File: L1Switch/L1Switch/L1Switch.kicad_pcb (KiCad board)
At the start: 4 copper layers, 191 parts, among them J1 RJSNEGF8A08, J2 Conn_01x07_Male, J3 Barrel_Jack, T1 SM51589PEL, T2 SM51589PEL, T3 SM51589PEL, T4 SM51589PEL, T5 SM51589PEL, T6 SM51589PEL, T7 SM51589PEL, T8 SM51589PEL, U1 XC7A15T-FTG256, U2 VSC8658, U3 TPS548A20RVE, U4 TPS565208, U5 TPS565208, U6 TPS565208

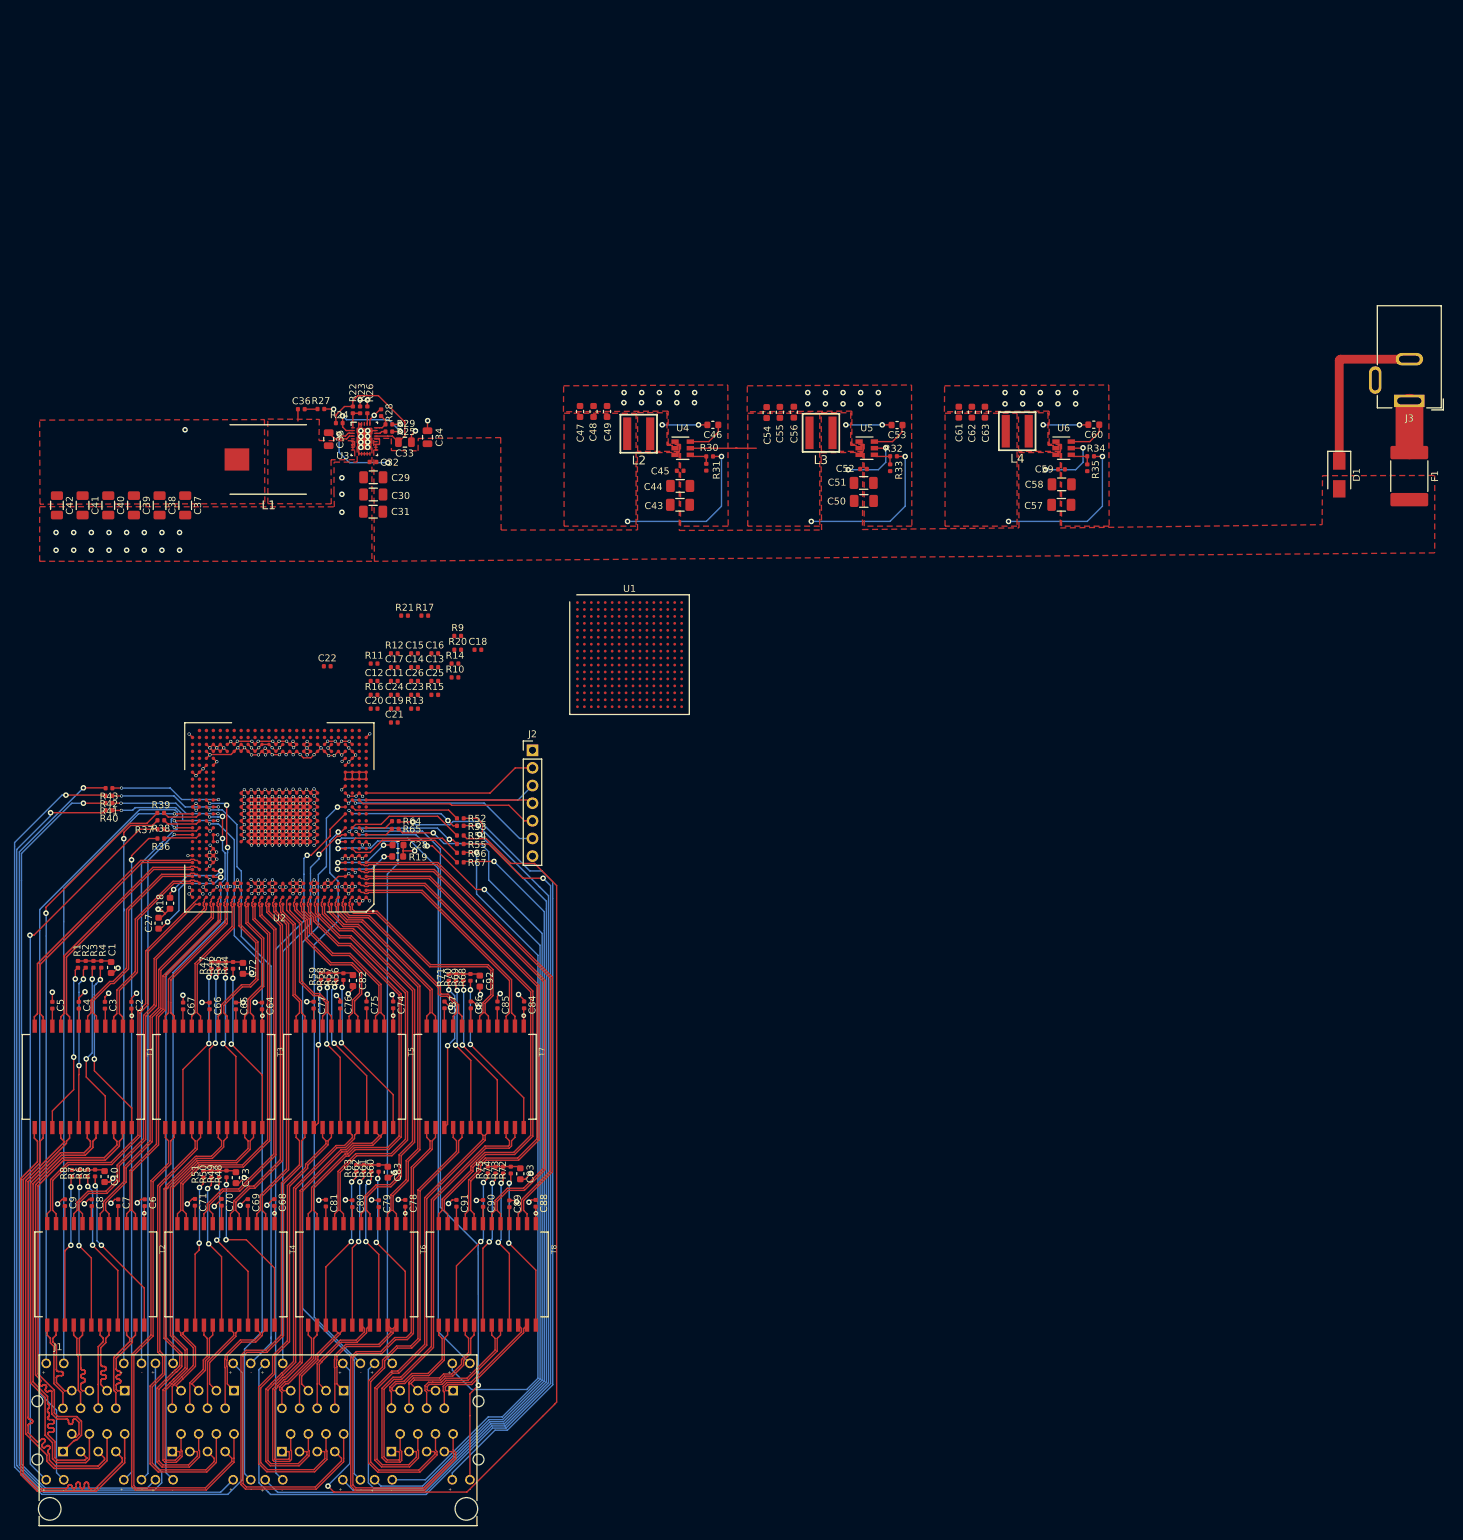
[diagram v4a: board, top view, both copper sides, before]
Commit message: SGMII 0 Rx/Tx routed to FPGA.
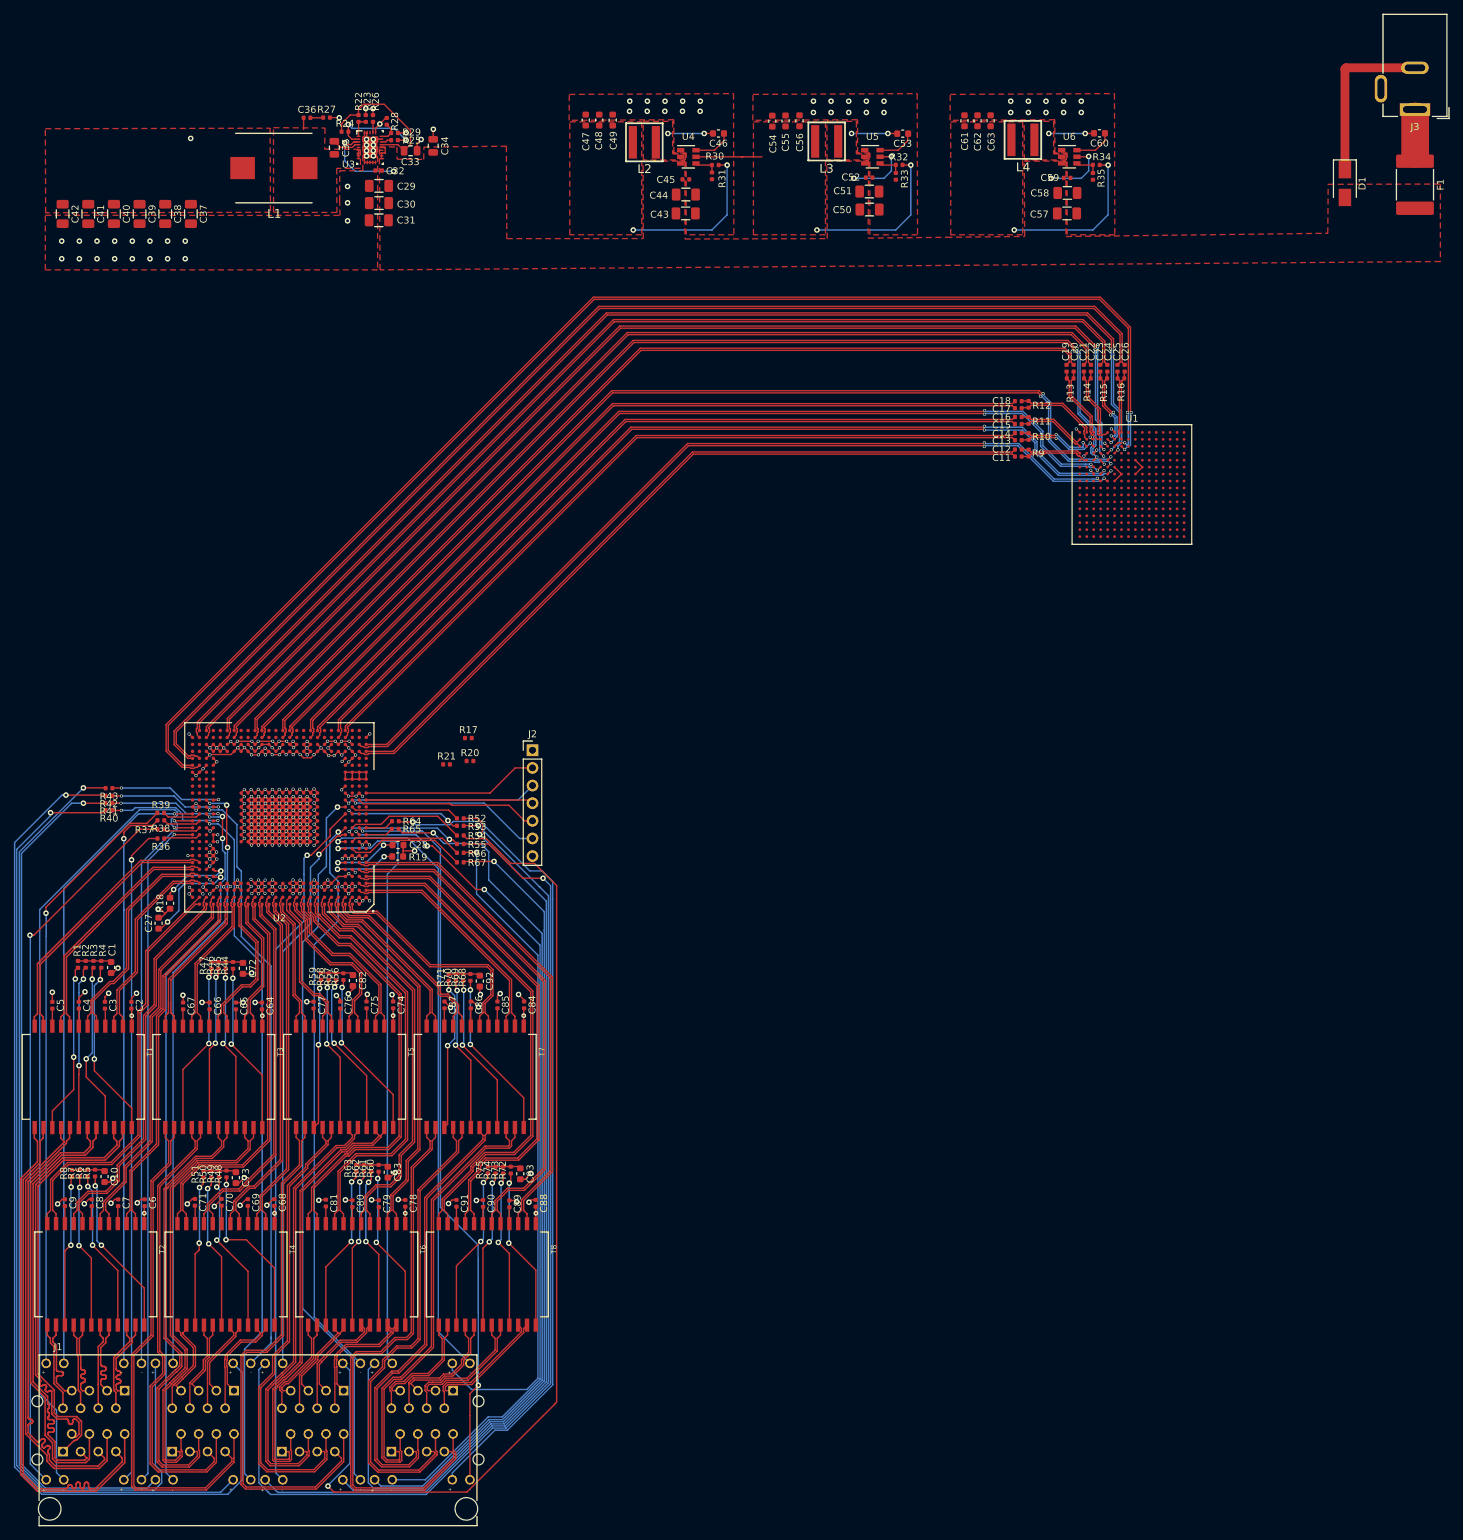
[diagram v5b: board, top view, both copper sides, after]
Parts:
- moved C22 118.0 mm to (224.1, -11.7), turned to 90 degrees
- moved R16 116.7 mm to (228.4, -10.3), turned to 180 degrees
- moved C24 112.9 mm to (226.5, -11.7), turned to 90 degrees
- moved C20 112.0 mm to (221.6, -11.7), turned to 90 degrees
- moved C26 111.7 mm to (229.0, -11.7), turned to 90 degrees
- moved C21 111.6 mm to (223.1, -11.7), turned to 90 degrees
- moved C23 109.3 mm to (225.4, -11.7), turned to 90 degrees
- moved C19 108.5 mm to (220.6, -11.7), turned to 90 degrees
- moved C25 108.1 mm to (227.9, -11.7), turned to 90 degrees
- moved R15 106.5 mm to (225.9, -10.3), turned to 180 degrees
- moved R13 105.7 mm to (221.1, -10.3), turned to 180 degrees
- moved R11 100.5 mm to (215.1, -4.22), turned to -90 degrees
- moved R14 99.9 mm to (223.6, -10.3), turned to 180 degrees
- moved C12 98.5 mm to (213.6, -0.04), turned to 180 degrees
- moved R12 98.1 mm to (215.1, -6.54), turned to -90 degrees
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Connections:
- net Net-(C11-Pad2) renamed /Net 1/RD_P7
- net Net-(C12-Pad2) renamed /Net 1/RD_N7
- net Net-(C13-Pad2) renamed /Net 1/RD_P6
- net Net-(C14-Pad2) renamed /Net 1/RD_N6
- net Net-(C15-Pad2) renamed /Net 1/RD_P5
- net Net-(C16-Pad2) renamed /Net 1/RD_N5
- net Net-(C17-Pad2) renamed /Net 1/RD_P4
- net Net-(C18-Pad2) renamed /Net 1/RD_N4
- net Net-(C19-Pad2) renamed /Net 1/RD_P3
- net Net-(C20-Pad2) renamed /Net 1/RD_N3
- net Net-(C21-Pad2) renamed /Net 1/RD_P2
- net Net-(C22-Pad2) renamed /Net 1/RD_N2
- net Net-(C23-Pad2) renamed /Net 1/RD_P1
- net Net-(C24-Pad2) renamed /Net 1/RD_N1
- net Net-(C25-Pad2) renamed /Net 1/RD_P0
- net Net-(C26-Pad2) renamed /Net 1/RD_N0
- C24 pad 1: /SGMII.RD_P0 -> /SGMII.RD_N1
- C25 pad 1: /SGMII.RD_N1 -> /SGMII.RD_P0
- R15 pad 1: /SGMII.RD_P0 -> /SGMII.RD_N1
- R16 pad 2: /SGMII.RD_N1 -> /SGMII.RD_P0
- U1 pad A2: Net-(U1-PadA2) -> /SGMII.RD_N4
- U1 pad A3: Net-(U1-PadA3) -> /SGMII.RD_N3
- U1 pad A4: Net-(U1-PadA4) -> /SGMII.RD_N2
- U1 pad A5: Net-(U1-PadA5) -> /SGMII.RD_P2
- U1 pad A7: Net-(U1-PadA7) -> /SGMII.RD_N0
- U1 pad B1: Net-(U1-PadB1) -> /SGMII.RD_N5
- U1 pad B2: Net-(U1-PadB2) -> /SGMII.RD_P4
- U1 pad B4: Net-(U1-PadB4) -> /SGMII.RD_P3
- U1 pad B5: Net-(U1-PadB5) -> /SGMII.RD_N1
- U1 pad B6: Net-(U1-PadB6) -> /SGMII.RD_P1
- U1 pad B7: Net-(U1-PadB7) -> /SGMII.RD_P0
- U1 pad C1: Net-(U1-PadC1) -> /SGMII.RD_P5
- U1 pad C2: Net-(U1-PadC2) -> /SGMII.RD_N6
- U1 pad C3: Net-(U1-PadC3) -> /SGMII.RD_P6
- U1 pad C4: Net-(U1-PadC4) -> /SGMII.TD_N2
- U1 pad C6: Net-(U1-PadC6) -> /SGMII.TD_N0
- U1 pad C7: Net-(U1-PadC7) -> /SGMII.TD_P0
- U1 pad D1: Net-(U1-PadD1) -> /SGMII.RD_N7
- U1 pad D16: /SGMII.RD_N7 -> Net-(U1-PadD16)
- U1 pad D3: Net-(U1-PadD3) -> /SGMII.TD_N3
- U1 pad D4: Net-(U1-PadD4) -> /SGMII.TD_P2
- U1 pad D5: Net-(U1-PadD5) -> /SGMII.TD_N1
- U1 pad D6: Net-(U1-PadD6) -> /SGMII.TD_P1
- U1 pad E15: /SGMII.RD_N6 -> Net-(U1-PadE15)
- U1 pad E16: /SGMII.RD_P7 -> Net-(U1-PadE16)
- U1 pad E2: Net-(U1-PadE2) -> /SGMII.RD_P7
- U1 pad E3: Net-(U1-PadE3) -> /SGMII.TD_P3
- U1 pad E5: Net-(U1-PadE5) -> /SGMII.TD_N4
- U1 pad F14: /SGMII.RD_N3 -> Net-(U1-PadF14)
- U1 pad F15: /SGMII.RD_P6 -> Net-(U1-PadF15)
- U1 pad F3: Net-(U1-PadF3) -> /SGMII.TD_N5
- U1 pad F4: Net-(U1-PadF4) -> /SGMII.TD_P5
- U1 pad F5: Net-(U1-PadF5) -> /SGMII.TD_P4
- U1 pad G12: /SGMII.RD_N5 -> Net-(U1-PadG12)
- U1 pad G14: /SGMII.RD_P3 -> Net-(U1-PadG14)
- U1 pad G15: /SGMII.RD_N0 -> Net-(U1-PadG15)
- U1 pad G16: /SGMII.RD_N2 -> Net-(U1-PadG16)
- U1 pad G4: Net-(U1-PadG4) -> /SGMII.TD_N6
- U1 pad G5: Net-(U1-PadG5) -> /SGMII.TD_P6
- U1 pad H11: /SGMII.RD_P5 -> Net-(U1-PadH11)
- U1 pad H12: /SGMII.RD_P4 -> Net-(U1-PadH12)
- U1 pad H13: /SGMII.RD_N4 -> Net-(U1-PadH13)
- U1 pad H14: /SGMII.RD_P0 -> Net-(U1-PadH14)
- U1 pad H16: /SGMII.RD_P2 -> Net-(U1-PadH16)
- U1 pad H4: Net-(U1-PadH4) -> /SGMII.TD_N7
- U1 pad H5: Net-(U1-PadH5) -> /SGMII.TD_P7
- U1 pad J15: /SGMII.RD_P1 -> Net-(U1-PadJ15)
- U1 pad J16: /SGMII.RD_N1 -> Net-(U1-PadJ16)
- U1 pad M6: /SGMII.TD_P5 -> Net-(U1-PadM6)
- U1 pad N6: /SGMII.TD_N5 -> Net-(U1-PadN6)
- U1 pad N9: /SGMII.TD_P6 -> Net-(U1-PadN9)
- U1 pad P8: /SGMII.TD_P4 -> Net-(U1-PadP8)
- U1 pad P9: /SGMII.TD_N6 -> Net-(U1-PadP9)
- U1 pad R10: /SGMII.TD_P7 -> Net-(U1-PadR10)
- U1 pad R11: /SGMII.TD_N7 -> Net-(U1-PadR11)
- U1 pad R5: /SGMII.TD_P1 -> Net-(U1-PadR5)
- U1 pad R6: /SGMII.TD_P0 -> Net-(U1-PadR6)
- U1 pad R7: /SGMII.TD_N0 -> Net-(U1-PadR7)
- U1 pad R8: /SGMII.TD_N4 -> Net-(U1-PadR8)
- U1 pad T10: /SGMII.TD_N2 -> Net-(U1-PadT10)
- U1 pad T5: /SGMII.TD_N1 -> Net-(U1-PadT5)
- U1 pad T7: /SGMII.TD_P3 -> Net-(U1-PadT7)
- U1 pad T8: /SGMII.TD_N3 -> Net-(U1-PadT8)
- U1 pad T9: /SGMII.TD_P2 -> Net-(U1-PadT9)
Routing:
- net /SGMII.TD_P0: track 0.00 -> 194.7 mm, vias 0 -> 2
- net /SGMII.TD_N0: track 0.00 -> 192.5 mm, vias 0 -> 2
- net /SGMII.TD_P1: track 0.00 -> 177.8 mm, vias 0 -> 2
- net /SGMII.TD_N1: track 0.00 -> 175.8 mm, vias 0 -> 2
- net /Net 1/RD_N0: track 0.00 -> 173.5 mm
- net /Net 1/RD_P0: track 0.00 -> 173.2 mm
- net /SGMII.TD_P2: track 0.00 -> 168.6 mm, vias 0 -> 2
- net /SGMII.TD_N2: track 0.00 -> 167.5 mm, vias 0 -> 2
- net /SGMII.TD_P3: track 0.00 -> 161.4 mm, vias 0 -> 2
- net /SGMII.TD_N3: track 0.00 -> 160.6 mm, vias 0 -> 2
- net /Net 1/RD_P1: track 0.00 -> 159.2 mm
- net /Net 1/RD_N1: track 0.00 -> 159.0 mm
- net /Net 1/RD_P2: track 0.00 -> 150.7 mm
- net /Net 1/RD_N2: track 0.00 -> 150.5 mm
- net /SGMII.TD_P4: track 0.00 -> 149.4 mm, vias 0 -> 2
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
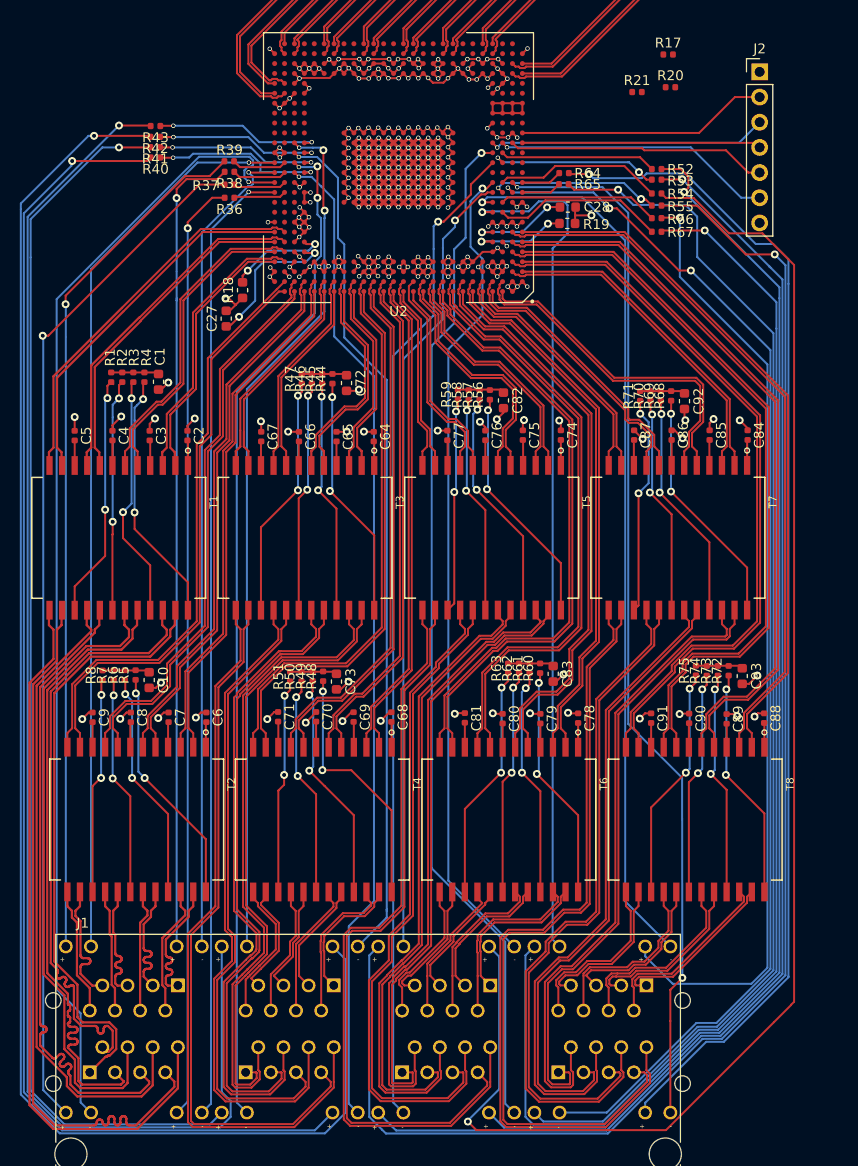
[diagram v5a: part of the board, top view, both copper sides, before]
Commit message: Add decoupling caps and ferrite bead. Clean up reference designators.
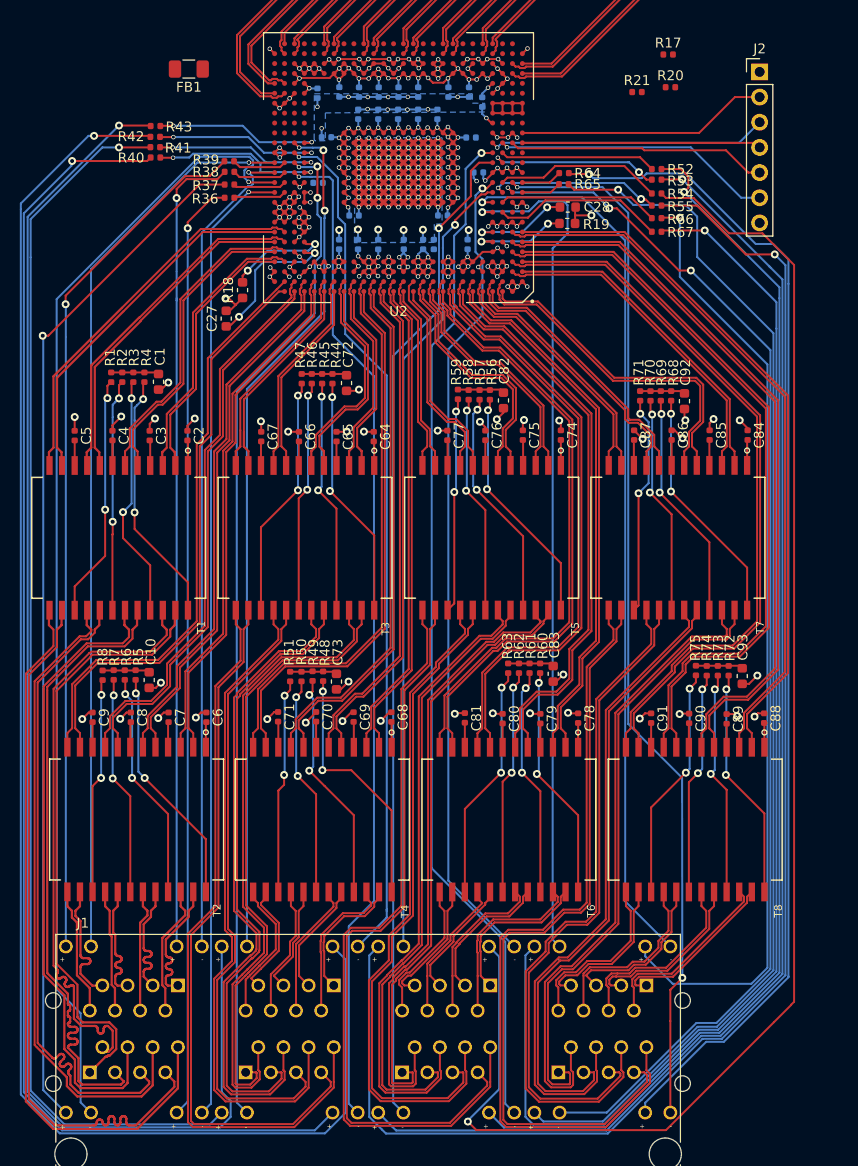
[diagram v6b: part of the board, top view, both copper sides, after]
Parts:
- added C100: 100nF, Capacitor_SMD:C_0402_1005Metric, B.Cu at (107.3, 45.3)
- added C101: 100nF, Capacitor_SMD:C_0402_1005Metric, B.Cu at (101.3, 60.7)
- added C102: 100nF, Capacitor_SMD:C_0402_1005Metric, B.Cu at (114.6, 49.9)
- added C103: 100nF, Capacitor_SMD:C_0402_1005Metric, B.Cu at (105.2, 47.5)
- added C104: 100nF, Capacitor_SMD:C_0402_1005Metric, B.Cu at (109.2, 47.5)
- added C105: 100nF, Capacitor_SMD:C_0402_1005Metric, B.Cu at (111.2, 47.5)
- added C106: 100nF, Capacitor_SMD:C_0402_1005Metric, B.Cu at (107.2, 47.5)
- added C107: 100nF, Capacitor_SMD:C_0402_1005Metric, B.Cu at (103.2, 47.5)
- added C108: 100nF, Capacitor_SMD:C_0402_1005Metric, B.Cu at (100.0, 49.9)
- added C109: 100nF, Capacitor_SMD:C_0402_1005Metric, B.Cu at (102.8, 57.8)
- added C110: 100nF, Capacitor_SMD:C_0402_1005Metric, B.Cu at (105.2, 60.7)
- added C111: 100nF, Capacitor_SMD:C_0402_1005Metric, B.Cu at (109.8, 60.7)
- added C112: 100nF, Capacitor_SMD:C_0402_1005Metric, B.Cu at (115.7, 46.3)
- added C113: 100nF, Capacitor_SMD:C_0402_1005Metric, B.Cu at (115.3, 53.4)
- added C114: 100nF, Capacitor_SMD:C_0402_1005Metric, B.Cu at (99.1, 45.4)
- added C115: 100nF, Capacitor_SMD:C_0402_1005Metric, B.Cu at (103.2, 60.7)
- added C116: 100nF, Capacitor_SMD:C_0402_1005Metric, B.Cu at (110.8, 60.7)
- added C117: 100nF, Capacitor_SMD:C_0402_1005Metric, B.Cu at (99.2, 54.5)
- added C118: 100nF, Capacitor_SMD:C_0402_1005Metric, B.Cu at (114.4, 45.3)
- added C119: 100nF, Capacitor_SMD:C_0402_1005Metric, B.Cu at (101.3, 45.3)
- added C120: 100nF, Capacitor_SMD:C_0402_1005Metric, B.Cu at (111.7, 57.7)
- added C94: 100nF, Capacitor_SMD:C_0402_1005Metric, B.Cu at (112.3, 45.3)
- added C95: 100nF, Capacitor_SMD:C_0402_1005Metric, B.Cu at (114.2, 60.7)
- added C96: 100nF, Capacitor_SMD:C_0402_1005Metric, B.Cu at (109.3, 45.3)
- added C97: 100nF, Capacitor_SMD:C_0402_1005Metric, B.Cu at (107.8, 60.7)
- added C98: 100nF, Capacitor_SMD:C_0402_1005Metric, B.Cu at (105.3, 45.3)
- added C99: 100nF, Capacitor_SMD:C_0402_1005Metric, B.Cu at (103.3, 45.3)
- added FB1: 100 ohm @ 100 MHz, 3A, L1Switch:FB_1206_3216Metric, F.Cu at (86.1, 43.0)
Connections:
- U2 pad H25: Net-(U2-PadH25) -> GND
- U2 pad J24: Net-(U2-PadJ24) -> GND
- U2 pad J25: Net-(U2-PadJ25) -> GND
- U2 pad J26: Net-(U2-PadJ26) -> GND
- U2 pad K24: Net-(U2-PadK24) -> GND
- U2 pad K25: Net-(U2-PadK25) -> GND
- U2 pad K26: Net-(U2-PadK26) -> GND
- U2 pad L24: Net-(U2-PadL24) -> GND
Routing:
- net GND: track 341.7 -> 385.4 mm, vias 216 -> 239
- net +1V2: track 69.7 -> 93.2 mm, vias 31 -> 43
- net +1V2A: track 46.8 -> 59.5 mm, vias 26 -> 29
- net +3V3: track 94.1 -> 105.7 mm, vias 52 -> 56
- net /Net 1/P3.LED0: track 100.4 -> 101.5 mm
- net /Net 1/P1.C-: track 65.1 -> 65.6 mm
- added copper zone on B.Cu, net GND
